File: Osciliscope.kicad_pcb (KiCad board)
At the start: 2 copper layers, 51 x 102 mm, 67 parts, among them J1 Conn_01x09_Socket, J2 Conn_01x04_Socket, J3 U.FL, J5 USB_C_Receptacle_USB2.0_14P, J6 Conn_01x02_MountingPin, J7 U.FL, J8 USB_C_Receptacle_USB2.0_14P, J9 Conn_01x03_Socket, SW1 RotaryEncoder_Switch, SW4 SW_Nidec_CAS-120A1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

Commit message: PCB updaes
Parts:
- removed SW4, SW7: SW_Nidec_CAS-120A1, Switch:SW_500SDP1S1M2QEA
- added J10: Conn_01x04_Socket, Connector_PinHeader_2.00mm:PinHeader_1x04_P2.00mm_Vertical, F.Cu at (107.8, 147.4)
- added J11: Conn_01x04_Socket, Connector_PinHeader_2.00mm:PinHeader_1x04_P2.00mm_Vertical, F.Cu at (101.8, 144.0)
- added J4: Conn_01x04_Socket, Connector_PinHeader_2.00mm:PinHeader_1x04_P2.00mm_Vertical, F.Cu at (141.2, 163.3)
- added R24: 10k, Capacitor_SMD:C_0603_1608Metric, F.Cu at (135.1, 153.7)
- C1, C10, C14, C15, C16, C17, C18, C19, C2, C20, C21, C3, C4, C5, C6, C7, C8, C9: footprint Capacitor_SMD:C_1206_3216Metric -> Capacitor_SMD:C_0402_1005Metric
- D5: footprint PCM_JLCPCB:D_0805 -> Capacitor_SMD:C_0603_1608Metric
- J5, J8: footprint Connector_USB:USB_C_Receptacle_Amphenol_124019772112A -> Connector_USB:USB_C_Receptacle_Amphenol_12401610E4-2A
- R13: value 10k -> 1k
- R19, R21, R22, R23: value 5.5k -> 5.1k
- U2: footprint Package_SO:VSSOP-8_3x3mm_P0.65mm -> ADC082S101CIMM_NOPB:SOP65P490X110-8N
- U3: value CH340N -> MCP2221AxML; footprint Package_SO:JEITA_SOIC-8_3.9x4.9mm_P1.27mm -> Package_DFN_QFN:QFN-16-1EP_4x4mm_P0.65mm_EP2.5x2.5mm
- moved C10 59.2 mm to (137.7, 168.2)
- moved C2 56.0 mm to (156.9, 141.2), turned to 0 degrees
- moved C20 52.7 mm to (137.7, 170.2), turned to 0 degrees
- moved C1 51.7 mm to (156.9, 139.2)
- moved R14 48.2 mm to (134.2, 165.1), turned to 0 degrees
- moved C6 47.9 mm to (137.7, 162.3), turned to 0 degrees
- moved U1 45.6 mm to (152.7, 135.3)
- moved R13 43.9 mm to (143.3, 136.0), turned to 0 degrees
- moved D5 42.5 mm to (143.3, 133.4)
- moved C8 42.3 mm to (137.7, 164.2), turned to 0 degrees
- moved J6 41.4 mm to (157.5, 134.2), turned to 0 degrees
- moved U5 38.5 mm to (145.8, 163.7), turned to 0 degrees
- moved R18 37.5 mm to (134.2, 167.6), turned to 0 degrees
- moved J9 37.4 mm to (147.3, 134.2), turned to 0 degrees
- moved C9 35.1 mm to (137.7, 166.2)
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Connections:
- J8 pad A6: Net-(U3-UD+) -> Net-(U3-D+)
- J8 pad A7: Net-(U3-UD-) -> Net-(U3-D-)
- J8 pad B6: Net-(U3-UD+) -> Net-(U3-D+)
- J8 pad B7: Net-(U3-UD-) -> Net-(U3-D-)
- U3 pad 1: Net-(U3-UD+) -> Net-(J11-Pin_1)
- U3 pad 2: Net-(U3-UD-) -> Net-(J11-Pin_2)
- U3 pad 3: GND -> Net-(U3-~{RST})
- U3 pad 4: RTS -> Net-(J10-Pin_3)
- U3 pad 5: 5Vin -> Net-(J10-Pin_4)
- U3 pad 6: TXD -> Net-(J11-Pin_3)
- U3 pad 7: RXD -> Net-(J11-Pin_4)
- U3 pad 8: unconnected-(U3-V3-Pad8) -> Net-(J10-Pin_1)
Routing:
- net 5Vin: track 67.6 -> 0.00 mm, vias 2 -> 0
- net V3.3: track 136.8 -> 86.7 mm, vias 7 -> 3
- net GND: track 64.3 -> 23.3 mm, vias 17 -> 7
- net V1.65: track 52.6 -> 23.5 mm, vias 4 -> 3
- net Net-(J7-In): track 27.7 -> 0.00 mm
- net CHAN_1: track 29.0 -> 4.80 mm
- net RPI_DOUT: track 22.7 -> 0.00 mm
- net RPI_DIN: track 19.4 -> 0.00 mm
- net Net-(U3-UD-): track 18.5 -> 0.00 mm, vias 2 -> 0
- net RPI_CS: track 16.8 -> 0.00 mm, vias 2 -> 0
- net RPI_SCLK: track 16.3 -> 0.00 mm
- net Net-(J3-In): track 15.7 -> 0.00 mm
- net Net-(J10-Pin_2): track 0.00 -> 15.6 mm
- net Net-(C10-Pad1): track 15.0 -> 0.00 mm
- net Net-(U5--): track 14.5 -> 0.00 mm, vias 2 -> 0
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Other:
- board size 51 x 102 mm -> 63.6 x 102 mm

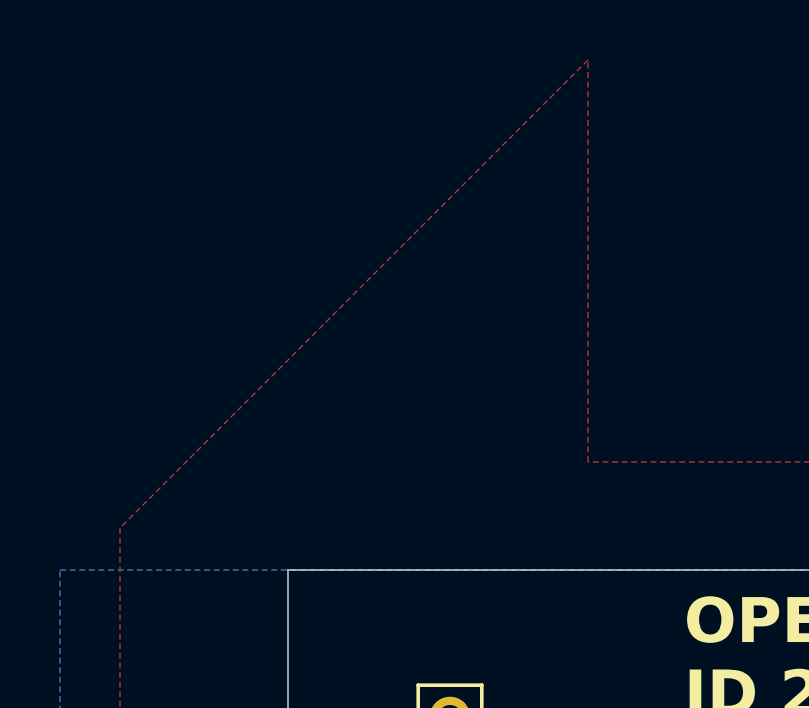
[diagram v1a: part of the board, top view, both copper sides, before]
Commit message: pcb board rules update
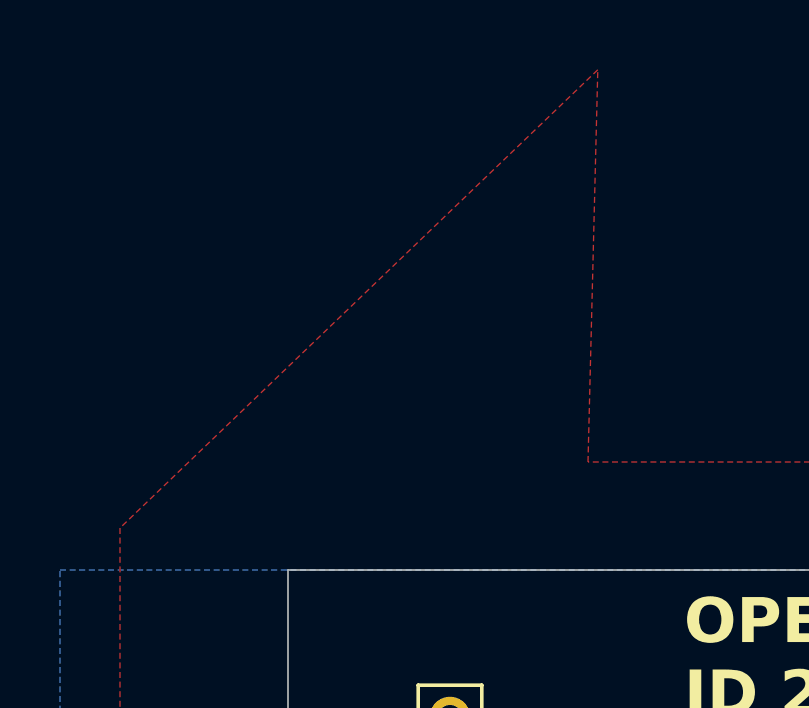
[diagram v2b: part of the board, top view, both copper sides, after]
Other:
- rule pad_to_mask_clearance: 0 -> 0.0508
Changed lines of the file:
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@@
 			(dielectric_constraints no)
 		)
-		(pad_to_mask_clearance 0)
+		(pad_to_mask_clearance 0.0508)
 		(allow_soldermask_bridges_in_footprints no)
 		(tenting front back)
@@
 			(pts
 				(xy 51.8 88.6) (xy 51.8 194) (xy 123.2 194) (xy 125.6 191.6) (xy 125.6 87.6) (xy 124.4 86.4) (xy 67.4 86.4)
-				(xy 67.4 73)
+				(xy 67.726353 73.326353)
 			)
 		)

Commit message: PCB Updates
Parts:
- removed J4: Conn_01x04_Socket, Connector_PinHeader_2.00mm:PinHeader_1x04_P2.00mm_Vertical
- moved J9 81.3 mm to (66.4, 142.8), turned to 90 degrees
- moved C20 67.2 mm to (70.6, 166.8), turned to 180 degrees
- moved R14 64.1 mm to (70.2, 168.6), turned to 180 degrees
- moved R18 57.7 mm to (76.6, 164.4), turned to -90 degrees
- moved J6 55.8 mm to (102.2, 127.0), turned to 180 degrees
- moved R3 55.7 mm to (78.6, 164.4), turned to 90 degrees
- moved C2 54.5 mm to (103.0, 133.0), turned to -135 degrees
- moved C1 54.1 mm to (103.6, 130.2), turned to 90 degrees
- moved C10 48.4 mm to (89.8, 175.2)
- moved C21 48.4 mm to (89.8, 179.2)
- moved C6 48.4 mm to (89.8, 169.3)
- moved C8 48.4 mm to (89.8, 171.3)
- moved C9 48.4 mm to (89.8, 173.3)
- moved R20 48.4 mm to (86.4, 179.6)
- moved TP1 48.4 mm to (97.8, 175.5)
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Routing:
- net V3.3: track 86.7 -> 35.6 mm, vias 3 -> 5
- net 5Vin: track 0.00 -> 46.8 mm
- net GND: track 23.3 -> 58.8 mm, vias 7 -> 22
- net CHAN_2: track 29.6 -> 2.63 mm
- net V1.65: track 23.5 -> 0.00 mm, vias 3 -> 0
- net Trig_clk: track 24.6 -> 47.7 mm
- net Net-(J3-In): track 0.00 -> 17.3 mm
- net Trig_dt: track 29.1 -> 43.2 mm
- net Net-(J5-CC2): track 0.00 -> 9.75 mm, vias 0 -> 2
- net Net-(J8-CC2): track 0.00 -> 9.37 mm
- net Net-(U7--): track 9.27 -> 0.00 mm
- net RPI_SCLK: track 0.00 -> 8.94 mm
- net V1.65RAW: track 8.90 -> 0.00 mm
- net Net-(J5-CC1): track 0.00 -> 7.98 mm, vias 0 -> 2
- net Net-(J8-CC1): track 0.00 -> 7.44 mm
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- added copper zone on F.Cu, net V3.3
- removed copper zone on F.Cu, net GND

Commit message: pcb updates and footprints
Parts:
- added J4: Conn_01x04_Socket, Connector_PinHeader_2.00mm:PinHeader_1x04_P2.00mm_Vertical, F.Cu at (157.4, 141.9)
- added S1: 500SDP1S1M2QEA, Switch:SW_500SDP1S1M2QEA, F.Cu at (148.3, 146.4)
- added S2: 500SDP1S1M2QEA, Switch:SW_500SDP1S1M2QEA, F.Cu at (149.3, 125.4)
- added S3: GF-123-0054, GF-123-0054:SW_GF-123-0054, F.Cu at (32.6, 135.1)
- moved J9 41.8 mm to (25.1, 149.3)
- moved C10 3.92 mm to (85.9, 175.0)
- moved C9 3.14 mm to (86.7, 173.2)
- moved C8 0.12 mm to (89.9, 171.4)

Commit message: more updates
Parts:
- moved S3 60.7 mm to (92.7, 126.3), turned to 90 degrees
- moved C2 3.32 mm to (102.1, 129.8), turned to 90 degrees
- moved TP5 3.04 mm to (101.3, 133.6)
- moved C1 0.40 mm to (103.6, 129.8)
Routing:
- net V3.3: track 35.6 -> 42.8 mm
- net GND: track 58.8 -> 59.9 mm, vias 22 -> 21

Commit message: more small changes
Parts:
- removed J9: Conn_01x03_Socket, Connector_PinSocket_2.00mm:PinSocket_1x03_P2.00mm_Vertical

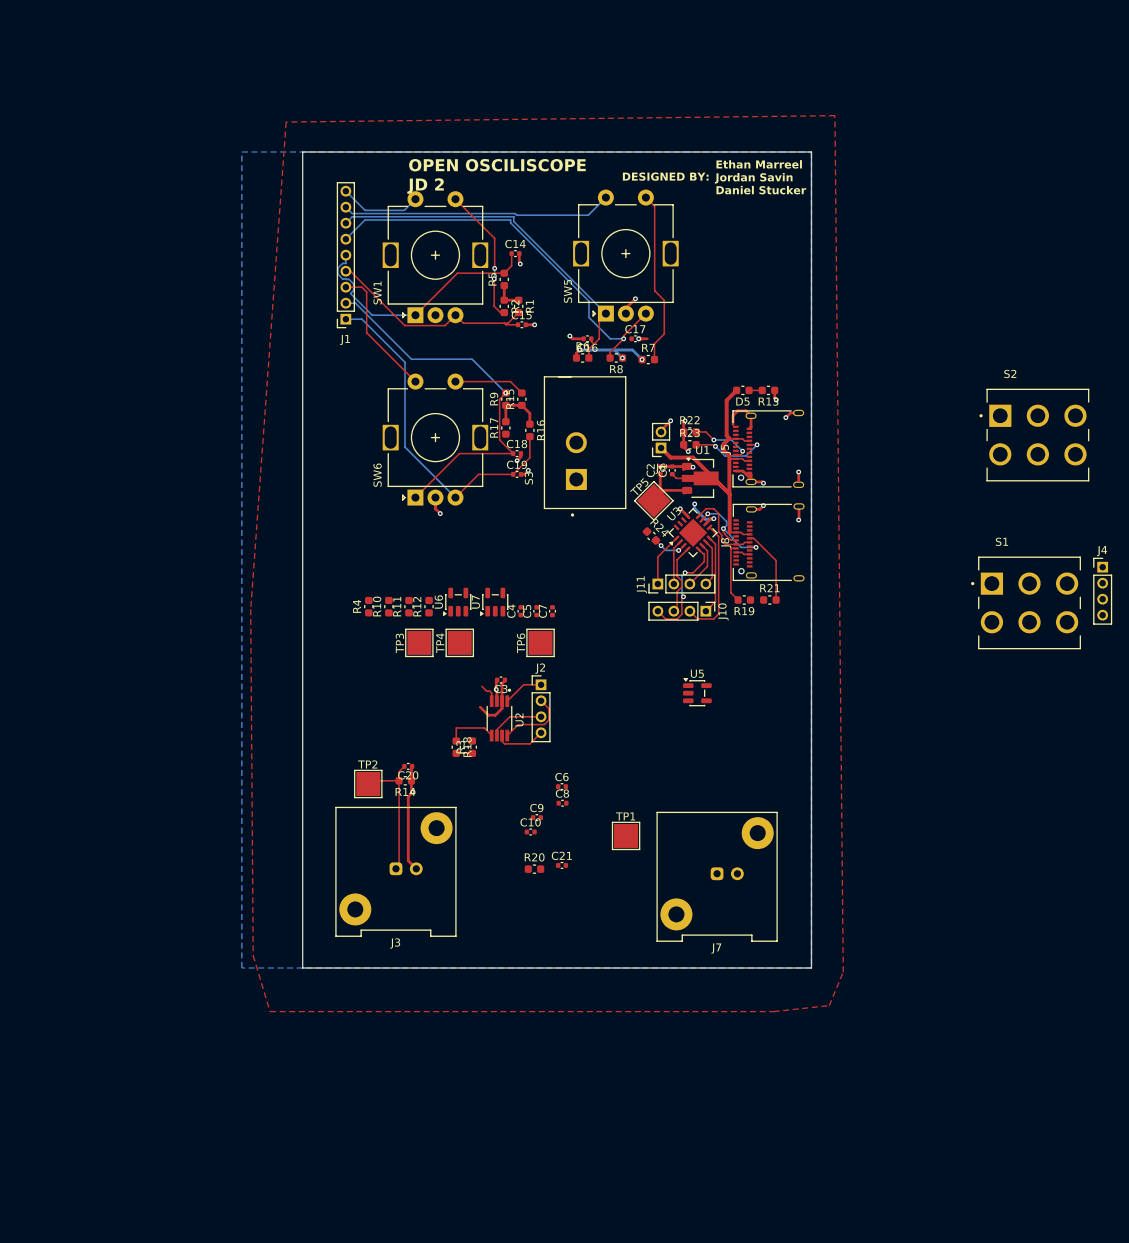
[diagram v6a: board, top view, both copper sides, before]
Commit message: footprints populated to PCB
there is an error tho lol
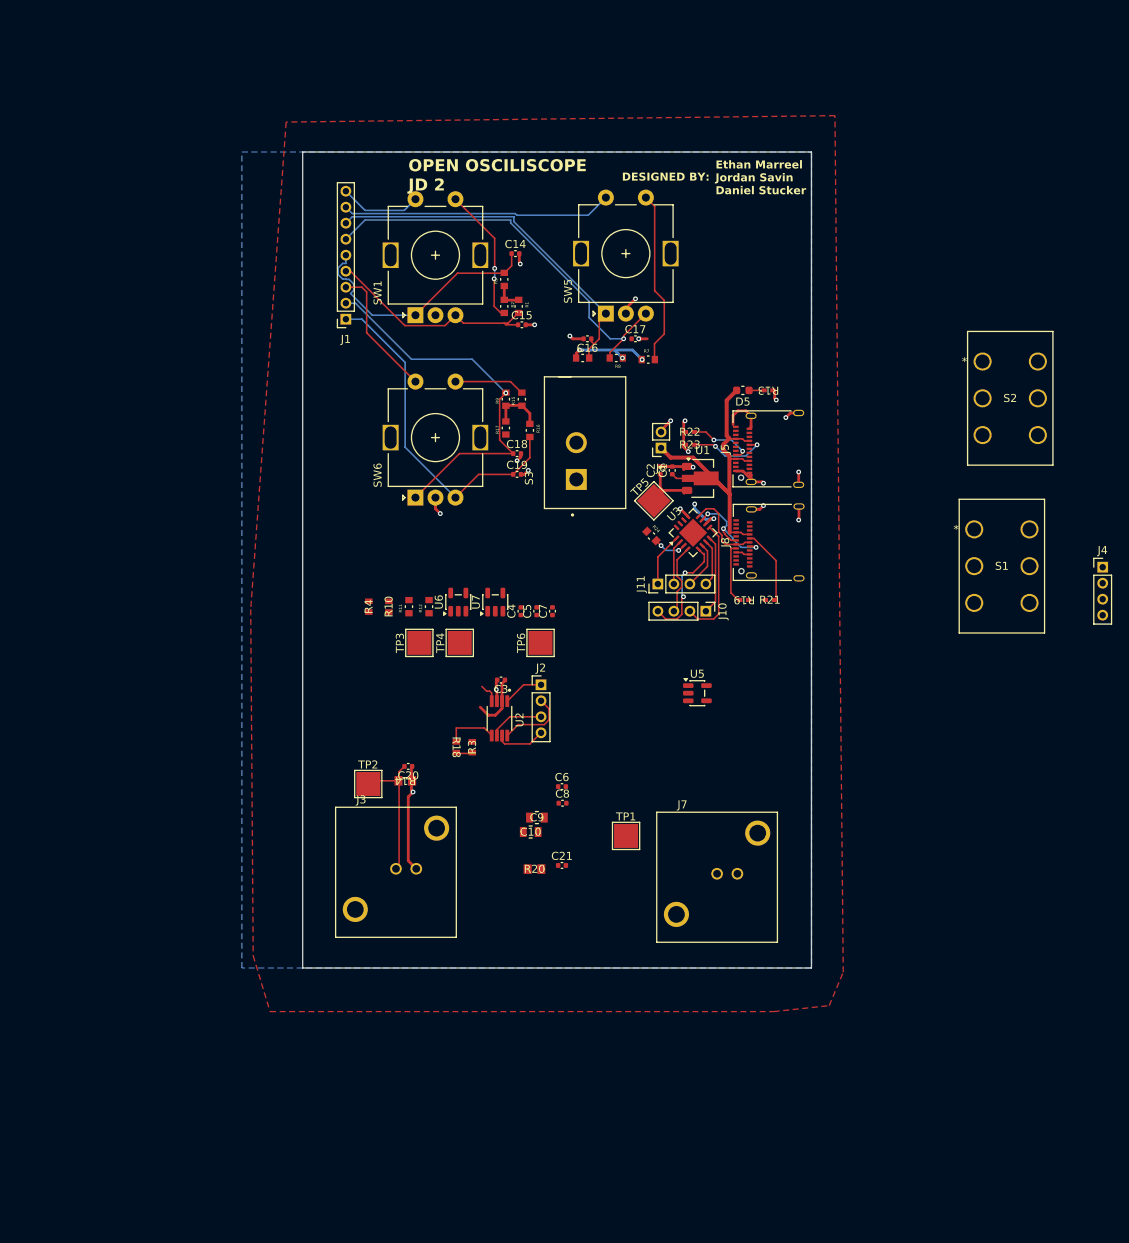
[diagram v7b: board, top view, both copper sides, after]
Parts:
- C10, C9: footprint Capacitor_SMD:C_0402_1005Metric -> SCOPE_FOOTPRINTS:CAP_CL21_SAM
- J3, J7: footprint Connector_Coaxial:BNC_Amphenol_031-5539_Vertical -> SCOPE_FOOTPRINTS:TE_5227671-1
- R1, R11, R12, R15, R16, R17, R2, R24, R5, R6, R7, R8, R9: footprint Capacitor_SMD:C_0603_1608Metric -> SCOPE_FOOTPRINTS:RESC1608X55N
- R10, R18, R3, R4: footprint Capacitor_SMD:C_0603_1608Metric -> SCOPE_FOOTPRINTS:RES_CRCW_0603
- R13, R19, R21, R22, R23: footprint Capacitor_SMD:C_0603_1608Metric -> SCOPE_FOOTPRINTS:RC0402N_PAN
- R14, R20: footprint Capacitor_SMD:C_0603_1608Metric -> SCOPE_FOOTPRINTS:RC0805N_PAN
- S1, S2: footprint Switch:SW_500SDP1S1M2QEA -> SCOPE_FOOTPRINTS:SWITCH_126-0327

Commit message: Routed
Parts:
- removed J4: Conn_01x04_Socket, Connector_PinHeader_2.00mm:PinHeader_1x04_P2.00mm_Vertical
- removed S3: GF-123-0054, GF-123-0054:SW_GF-123-0054
- C10, C9: footprint SCOPE_FOOTPRINTS:CAP_CL21_SAM -> Capacitor_SMD:C_0402_1005Metric
- J3, J7: footprint SCOPE_FOOTPRINTS:TE_5227671-1 -> Connector_Coaxial:BNC_Amphenol_031-5539_Vertical
- R1, R11, R12, R15, R16, R17, R2, R24, R5, R6, R7, R8, R9: footprint SCOPE_FOOTPRINTS:RESC1608X55N -> Capacitor_SMD:C_0603_1608Metric
- R10, R18, R3, R4: footprint SCOPE_FOOTPRINTS:RES_CRCW_0603 -> Capacitor_SMD:C_0603_1608Metric
- R13, R19, R21, R22, R23: footprint SCOPE_FOOTPRINTS:RC0402N_PAN -> Capacitor_SMD:C_0603_1608Metric
- R14, R20: footprint SCOPE_FOOTPRINTS:RC0805N_PAN -> Capacitor_SMD:C_0603_1608Metric
- moved S1 75.3 mm to (73.8, 157.5), turned to 90 degrees
- moved S2 58.7 mm to (104.8, 163.6), turned to -90 degrees
- moved C10 31.9 mm to (63.2, 152.5), turned to -90 degrees
- moved TP1 29.3 mm to (114.2, 151.2)
- moved C9 25.7 mm to (111.7, 167.2)
- moved TP4 24.1 mm to (98.4, 162.6), turned to 0 degrees
- moved R18 22.4 mm to (97.6, 156.6)
- moved R3 22.4 mm to (99.6, 156.6)
- moved R20 22.1 mm to (105.4, 168.4)
- moved C21 17.7 mm to (105.3, 170.6)
- moved R11 16.5 mm to (86.8, 150.4)
- moved R10 13.2 mm to (80.0, 152.8)
- moved TP3 13.2 mm to (84.8, 154.4), turned to 0 degrees
- moved R12 12.1 mm to (84.8, 150.4)
- moved U5 11.9 mm to (96.6, 151.5), turned to 90 degrees
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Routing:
- net Net-(J7-In): track 0.00 -> 49.6 mm
- net V1.65: track 0.00 -> 34.4 mm, vias 0 -> 5
- net Net-(C10-Pad1): track 0.00 -> 27.5 mm
- net CHAN_1: track 6.43 -> 30.3 mm
- net V3.3: track 42.8 -> 63.3 mm
- net CHAN_2: track 2.63 -> 19.7 mm
- net GND: track 59.9 -> 75.8 mm, vias 21 -> 27
- net Net-(C9-Pad1): track 0.00 -> 13.6 mm
- net Net-(R3-Pad2): track 0.00 -> 13.2 mm
- net Net-(S2-Pad1): track 0.00 -> 12.1 mm
- net Net-(S1-Pad1): track 0.00 -> 12.1 mm
- net V1.65RAW: track 0.00 -> 12.0 mm
- net Net-(U7--): track 0.00 -> 11.6 mm
- net Net-(U5--): track 2.00 -> 9.87 mm
- net Net-(J3-In): track 17.3 -> 22.7 mm
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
